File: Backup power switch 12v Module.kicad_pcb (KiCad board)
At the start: 2 copper layers, 94.3 x 76.2 mm, 58 parts, among them J1 BAT/PWR IN, J2 External, J3 PWR OUT, J4 Barrel_Jack_MountingPin, J5 Esternal, J6 Barrel_Jack_MountingPin, J7 Barrel_Jack_MountingPin, J8 Barrel_Jack_MountingPin, J9 PWR SELECTOR, K1 SRD-12VDC-SL-C, Q2 AO3401A, Q3 BSS138, U2 INA219AxD, U3 INA219AxD, U4 LTV-817, U5 LTV-817, U6 CN3763, U7 ESP32-C3 Pro Mini, U8 AMS1117-3.3

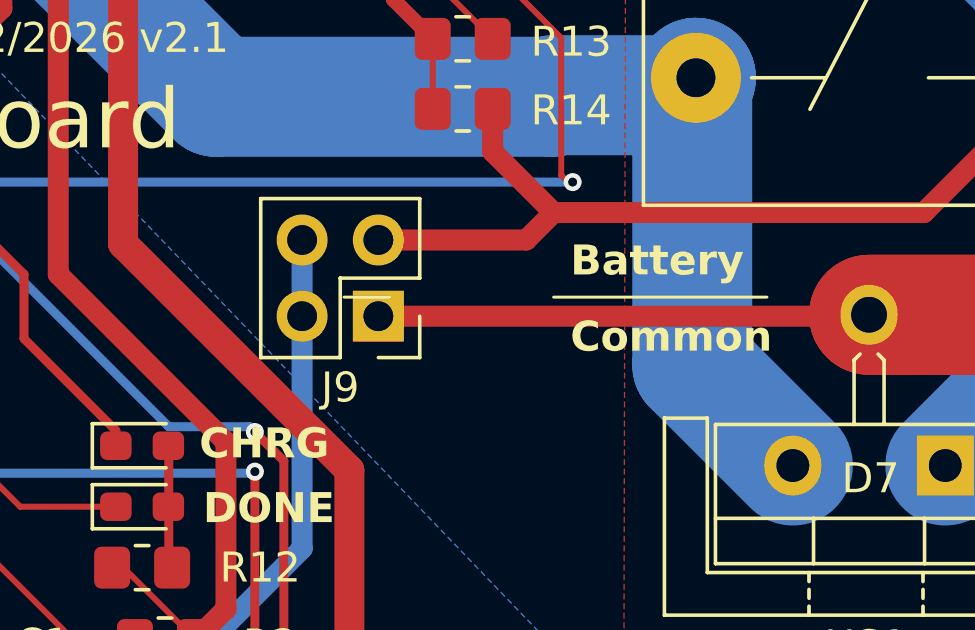
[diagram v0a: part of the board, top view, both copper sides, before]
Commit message: Fix charger in/out nammes
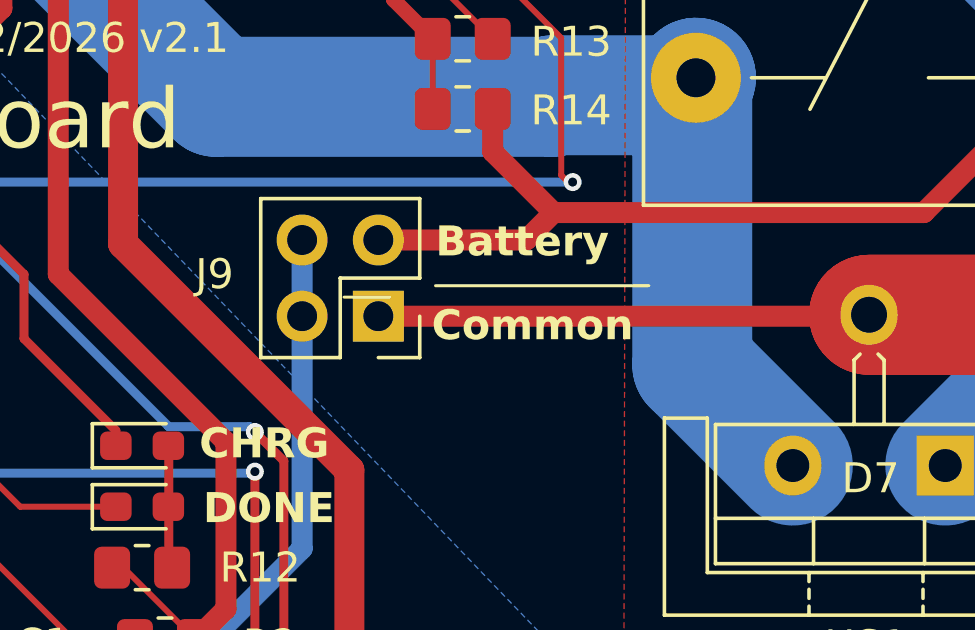
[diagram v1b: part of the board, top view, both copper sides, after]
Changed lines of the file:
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@@
 		(tags "Through hole pin header THT 2x02 2.54mm double row")
 		(property "Reference" "J9"
-			(at 1.27 -2.380001 0)
+			(at 5.461 1.397 0)
 			(layer "F.SilkS")
 			(effects
@@
 	)
 	(gr_line
-		(start 148.59 100.203)
-		(end 155.702 100.203)
+		(start 144.653 99.822)
+		(end 151.765 99.822)
 		(stroke
 			(width 0.1)
@@
 	)
 	(gr_text "Common"
-		(at 149.1488 102.108 0)
+		(at 144.526 101.727 0)
 		(layer "F.SilkS")
 		(effects
@@
 	)
 	(gr_text "Battery"
-		(at 149.1488 99.568 0)
+		(at 144.653 98.933 0)
 		(layer "F.SilkS")
 		(effects

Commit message: Production
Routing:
- net BAT OUT 12 +: track 101.6 -> 100.7 mm
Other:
- board text added: "Abel 03/2026 v3"
- board text removed: "Abel 02/2026 v2.1"
- board text removed: "gnd"
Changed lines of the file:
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@@
 		)
 	)
-	(gr_text "Abel 02/2026 v2.1"
+	(gr_text "Abel 03/2026 v3"
 		(at 125.1712 92.1512 0)
 		(layer "F.SilkS")
@@
 		)
 	)
-	(gr_text "gnd"
-		(at 121.3104 127.9652 90)
+	(gr_text "GND"
+		(at 121.3104 128.143 90)
 		(layer "F.SilkS")
 		(effects
@@
 	)
 	(segment
-		(start 112.395 106.045)
-		(end 104.511 113.929)
-		(width 0.3)
+		(start 148.844 96.139)
+		(end 148.844 91.562201)
+		(width 0.2)
 		(layer "F.Cu")
 		(net 18)
 	)
 	(segment
-		(start 148.844 96.139)
-		(end 148.844 91.562201)
-		(width 0.2)
+		(start 112.395 106.045)
+		(end 104.511 113.929)
+		(width 0.3)
 		(layer "F.Cu")
 		(net 18)
@@
 	)
 	(segment
-		(start 112.395 96.393)
-		(end 112.395 106.045)
+		(start 104.511 113.929)
+		(end 104.511 118.728)
 		(width 0.3)
 		(layer "F.Cu")
@@
 	)
 	(segment
-		(start 104.511 113.929)
-		(end 104.511 118.728)
-		(width 0.3)
+		(start 146.78 87.0712)
+		(end 146.78 89.012999)
+		(width 0.2)
 		(layer "F.Cu")
 		(net 18)
 	)
 	(segment
-		(start 146.78 87.0712)
-		(end 146.78 89.012999)
-		(width 0.2)
+		(start 112.395 96.393)
+		(end 112.395 106.045)
+		(width 0.3)
 		(layer "F.Cu")
 		(net 18)
@@
 	)
 	(segment
-		(start 149.225 96.3676)
-		(end 115.3414 96.3676)
+		(start 115.3414 96.3676)
+		(end 149.225 96.3676)
 		(width 0.3)
 		(layer "B.Cu")
@@
 	(segment
 		(start 115.316 96.393)
-		(end 112.395 96.393)
+		(end 115.3414 96.3676)
 		(width 0.3)
 		(layer "B.Cu")
@@
 	)
 	(segment
-		(start 115.3414 96.3676)
+		(start 112.395 96.393)
 		(end 115.316 96.393)
 		(width 0.3)
@@
 	)
 	(segment
-		(start 125.5268 80.264)
-		(end 124.46 81.3308)
-		(width 0.5)
+		(start 146.5608 95.3544)
+		(end 148.59 97.3836)
+		(width 0.7)
 		(layer "F.Cu")
 		(net 37)
 	)
 	(segment
-		(start 146.5608 95.3544)
-		(end 148.59 97.3836)
-		(width 0.7)
+		(start 125.5268 80.264)
+		(end 124.46 81.3308)
+		(width 0.5)
 		(layer "F.Cu")
 		(net 37)
@@
 	)
 	(segment
+		(start 131.953 80.899)
+		(end 131.318 80.264)
+		(width 0.5)
+		(layer "F.Cu")
+		(net 37)
+	)
+	(segment
+		(start 124.46 81.3308)
+		(end 124.46 83.25)
+		(width 0.5)
+		(layer "F.Cu")
+		(net 37)
+	)
+	(segment
 		(start 146.5608 93.9292)
 		(end 146.5608 95.3544)
@@
 	)
 	(segment
+		(start 131.318 80.264)
+		(end 125.5268 80.264)
+		(width 0.5)
+		(layer "F.Cu")
+		(net 37)
+	)
+	(segment
 		(start 141.732 77.216)
 		(end 141.732 77.47)
@@
 	)
 	(segment
-		(start 124.46 81.3308)
-		(end 124.46 83.25)
-		(width 0.5)
-		(layer "F.Cu")
-		(net 37)
-	)
-	(segment
 		(start 148.59 97.3836)
 		(end 147.6756 98.298)
@@
 		(net 37)
 	)
-	(segment
-		(start 131.953 80.264)
-		(end 125.5268 80.264)
-		(width 0.5)
-		(layer "F.Cu")
-		(net 37)
-	)
 	(via
 		(at 141.732 77.47)
@@
 	)
 	(via
-		(at 131.953 80.264)
+		(at 131.953 80.899)
 		(size 0.6)
 		(drill 0.3)
@@
 	)
 	(segment
-		(start 141.478 80.264)
-		(end 131.953 80.264)
-		(width 0.5)
-		(layer "B.Cu")
-		(net 37)
-	)
-	(segment
-		(start 141.732 77.47)
-		(end 141.732 80.01)
+		(start 131.953 80.899)
+		(end 132.588 80.264)
 		(width 0.5)
 		(layer "B.Cu")
@@
 	)
 	(segment
-		(start 165.385 90.5566)
-		(end 165.385 92.94)
-		(width 4)
+		(start 138.938 80.264)
+		(end 141.732 77.47)
+		(width 0.5)
 		(layer "B.Cu")
 		(net 37)
 	)
 	(segment
-		(start 141.732 80.01)
-		(end 141.478 80.264)
-		(width 0.5)
+		(start 165.385 90.5566)
+		(end 165.385 92.94)
+		(width 4)
 		(layer "B.Cu")
 		(net 37)
@@
 		(layer "B.Cu")
 		(net 37)
+	)
+	(segment
+		(start 132.588 80.264)
+		(end 138.938 80.264)
+		(width 0.5)
+		(layer "B.Cu")
+		(net 37)
